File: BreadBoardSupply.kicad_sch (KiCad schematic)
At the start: 17 parts, among them J1 Barrel_Jack_Switch, J2 Conn_01x02_Male, J3 Conn_01x03_Male, J4 Screw_Terminal_01x02, J5 Conn_01x02_Male, J6 Conn_01x03_Male, J7 Screw_Terminal_01x02, U1 LM7805_TO220, U2 LM317_TO-220

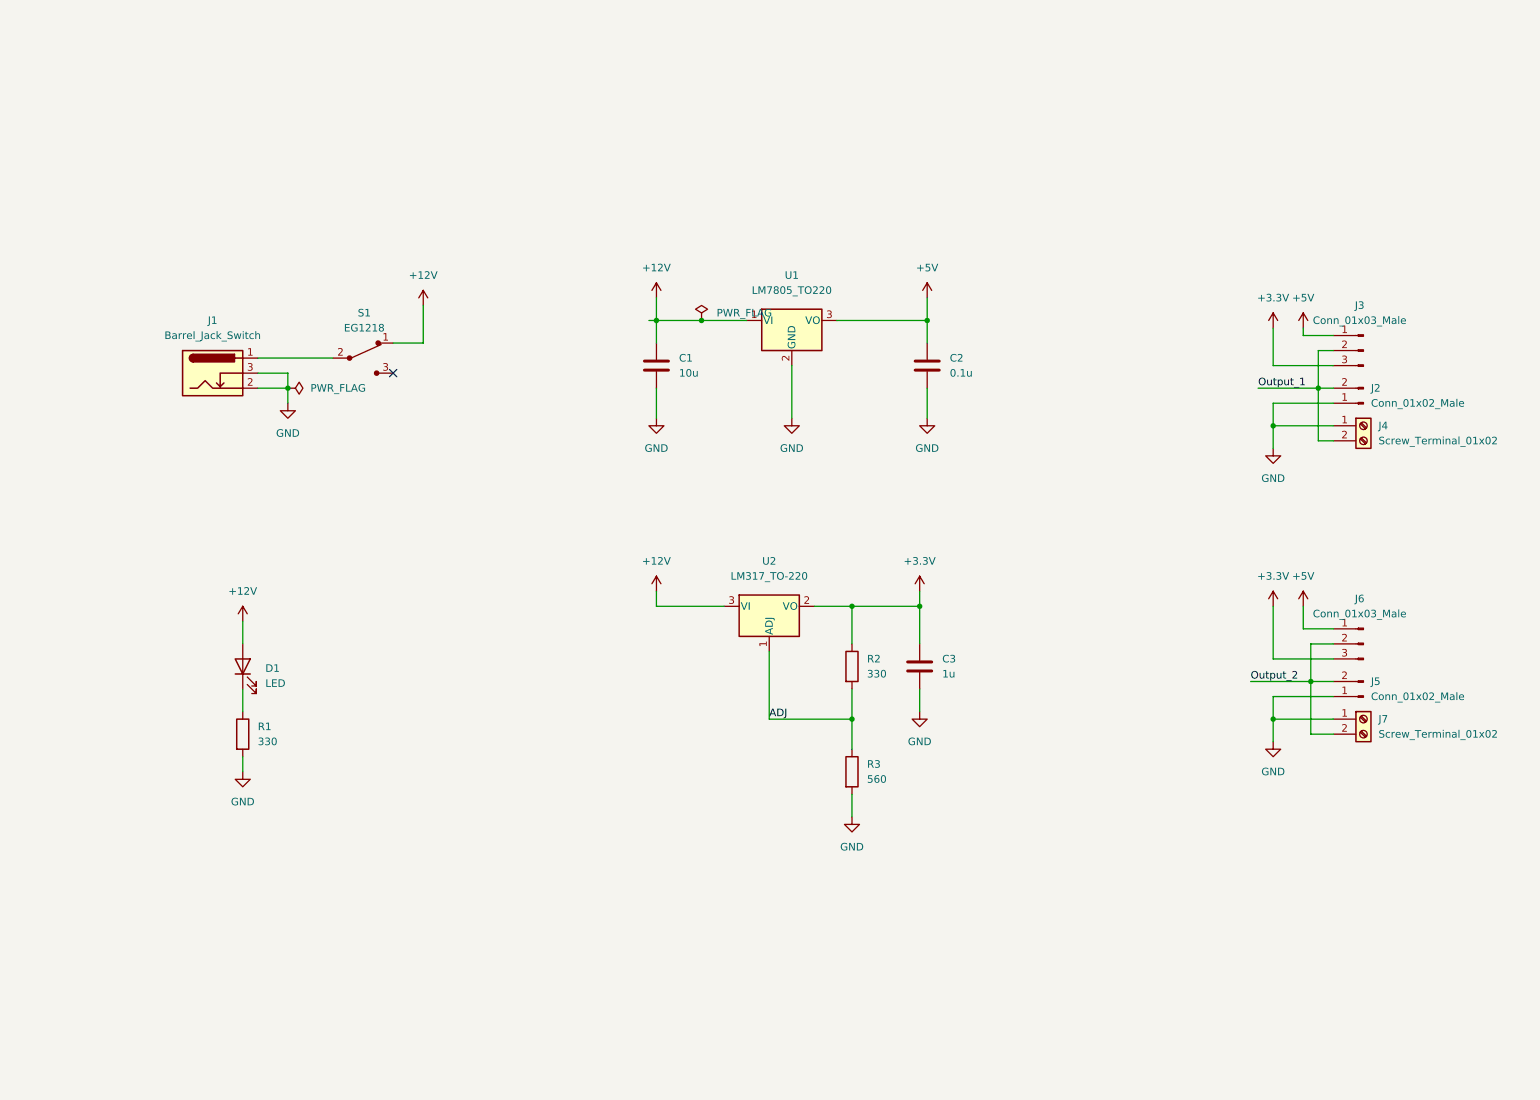
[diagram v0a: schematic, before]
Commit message: changed the footprints of some components, modified the regulator circuit
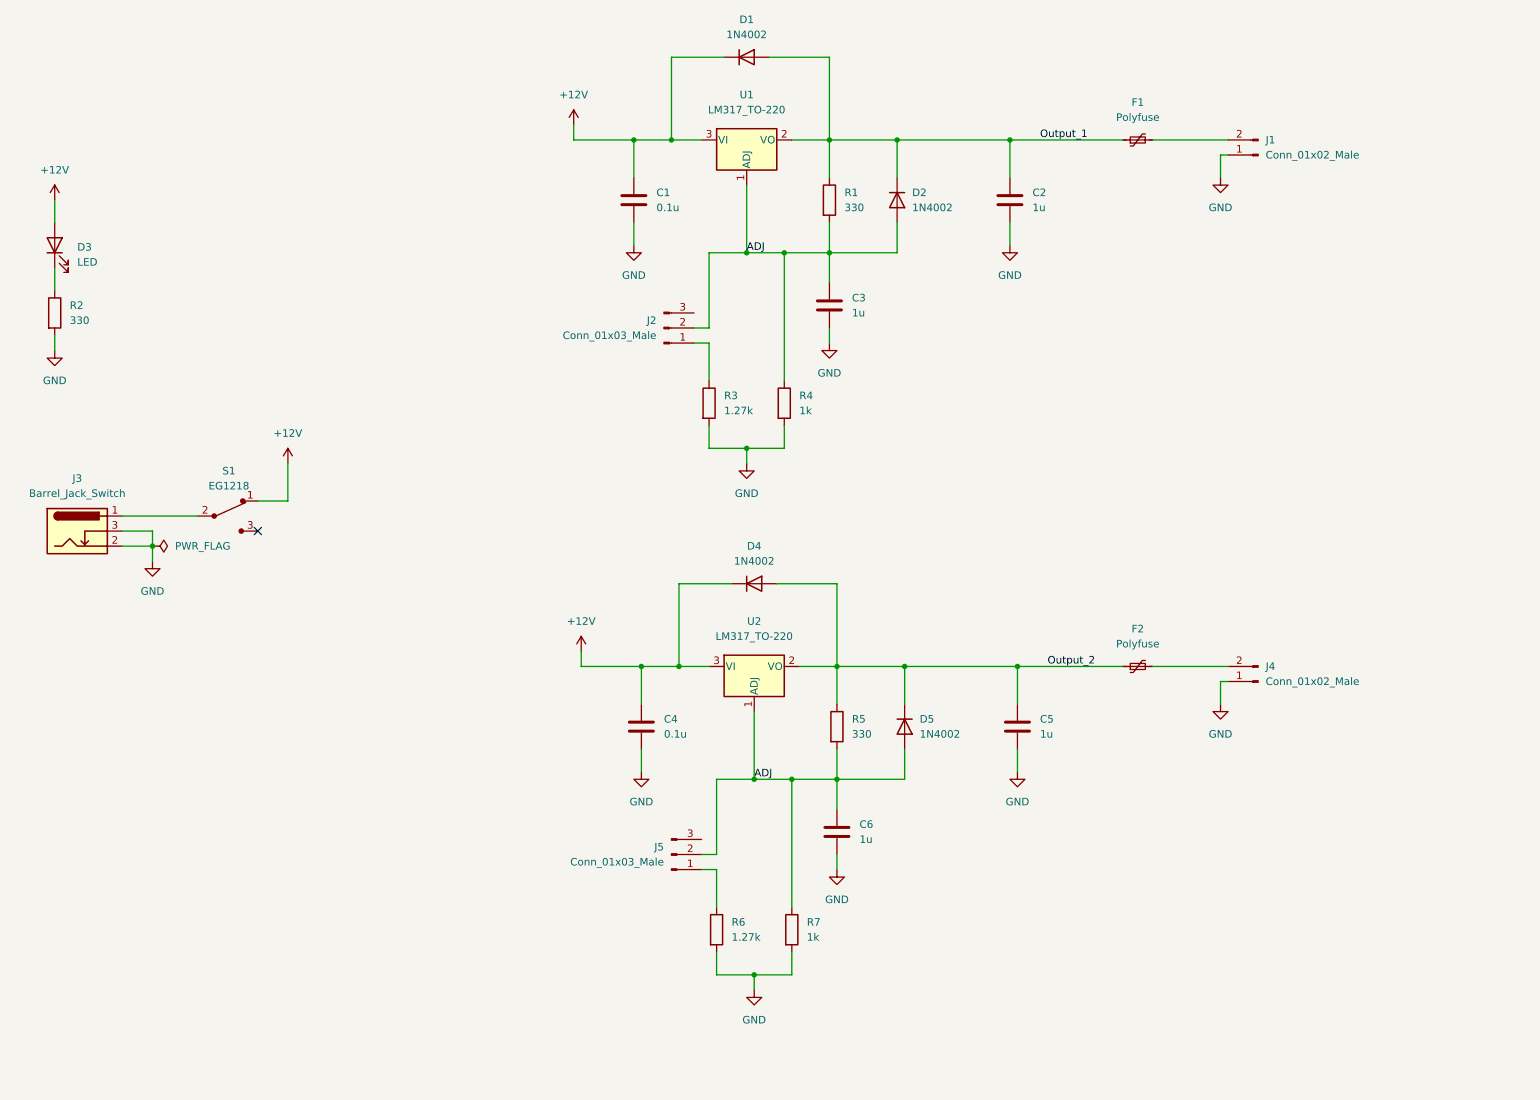
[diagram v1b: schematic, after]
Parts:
- removed J2: Conn_01x02_Male, Connector_PinHeader_2.54mm:PinHeader_1x02_P2.54mm_Vertical, symbol Connector:Conn_01x02_Male
- removed J3, J6: Conn_01x03_Male, Connector_PinHeader_2.54mm:PinHeader_1x03_P2.54mm_Vertical, symbol Connector:Conn_01x03_Male
- removed J4, J7: Screw_Terminal_01x02, TerminalBlock:TerminalBlock_bornier-2_P5.08mm, symbol Connector:Screw_Terminal_01x02
- removed U1: LM7805_TO220, Package_TO_SOT_THT:TO-220-3_Vertical, symbol Regulator_Linear:LM7805_TO220
- added C3, C6: 1u, Capacitor_THT:C_Disc_D3.0mm_W1.6mm_P2.50mm, symbol Device:C
- added C4: 0.1u, Capacitor_THT:C_Disc_D3.0mm_W1.6mm_P2.50mm, symbol Device:C
- added D1, D2, D4, D5: 1N4002, Diode_THT:D_DO-41_SOD81_P10.16mm_Horizontal, symbol Diode:1N4002
- added F1, F2: Polyfuse, symbol Device:Polyfuse_Small
- added J1: Conn_01x02_Male, Connector_PinHeader_2.54mm:PinHeader_1x02_P2.54mm_Vertical, symbol Connector:Conn_01x02_Male
- added J2, J5: Conn_01x03_Male, Connector_PinHeader_2.54mm:PinHeader_1x03_P2.54mm_Vertical, symbol Connector:Conn_01x03_Male
- added R1: 330, Resistor_THT:R_Axial_DIN0204_L3.6mm_D1.6mm_P7.62mm_Horizontal, symbol Device:R
- added R4, R7: 1k, Resistor_THT:R_Axial_DIN0204_L3.6mm_D1.6mm_P7.62mm_Horizontal, symbol Device:R
- added R6: 1.27k, Resistor_THT:R_Axial_DIN0204_L3.6mm_D1.6mm_P7.62mm_Horizontal, symbol Device:R
- added U1: LM317_TO-220, Package_TO_SOT_THT:TO-220-3_Vertical, symbol Regulator_Linear:LM317_TO-220
- C1: value 10u -> 0.1u
- C2: value 0.1u -> 1u
- R3: value 560 -> 1.27k
- renumbered C3 to C5, D1 to D3, J1 to J3, J5 to J4, R1 to R2, R2 to R5
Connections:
- net +3.3V is gone; now on net Output_2: C5.1, R5.1, U2.2 (VO)
- net +5V is gone; now on net Output_1: C2.1
- net +12V: now also C4.1, D1.1 (K), D4.1 (K), U1.3 (VI)
- net ADJ: now also C3.1, C6.1, D2.2 (A), D5.2 (A), J2.2 (Pin_2), J5.2 (Pin_2), R1.2, R4.1, R7.1, U1.1 (ADJ); no longer R3.1
- net GND: now also C3.2, C4.2, C6.2, J1.1 (Pin_1), R4.2, R6.2, R7.2
- net Output_1: now also D1.2 (A), D2.1 (K), F1.1, R1.1, U1.2 (VO)
- net Output_2: now also D4.2 (A), D5.1 (K), F2.1; no longer J4.2 (Pin_2)
- new net: J2.1 (Pin_1), R3.1
- new net: F2.2, J4.2 (Pin_2)
- new net: F1.2, J1.2 (Pin_2)
- new net: J5.1 (Pin_1), R6.1
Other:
- moved on the sheet: C5, D3, J3, J4, R2, R5, S1, U2

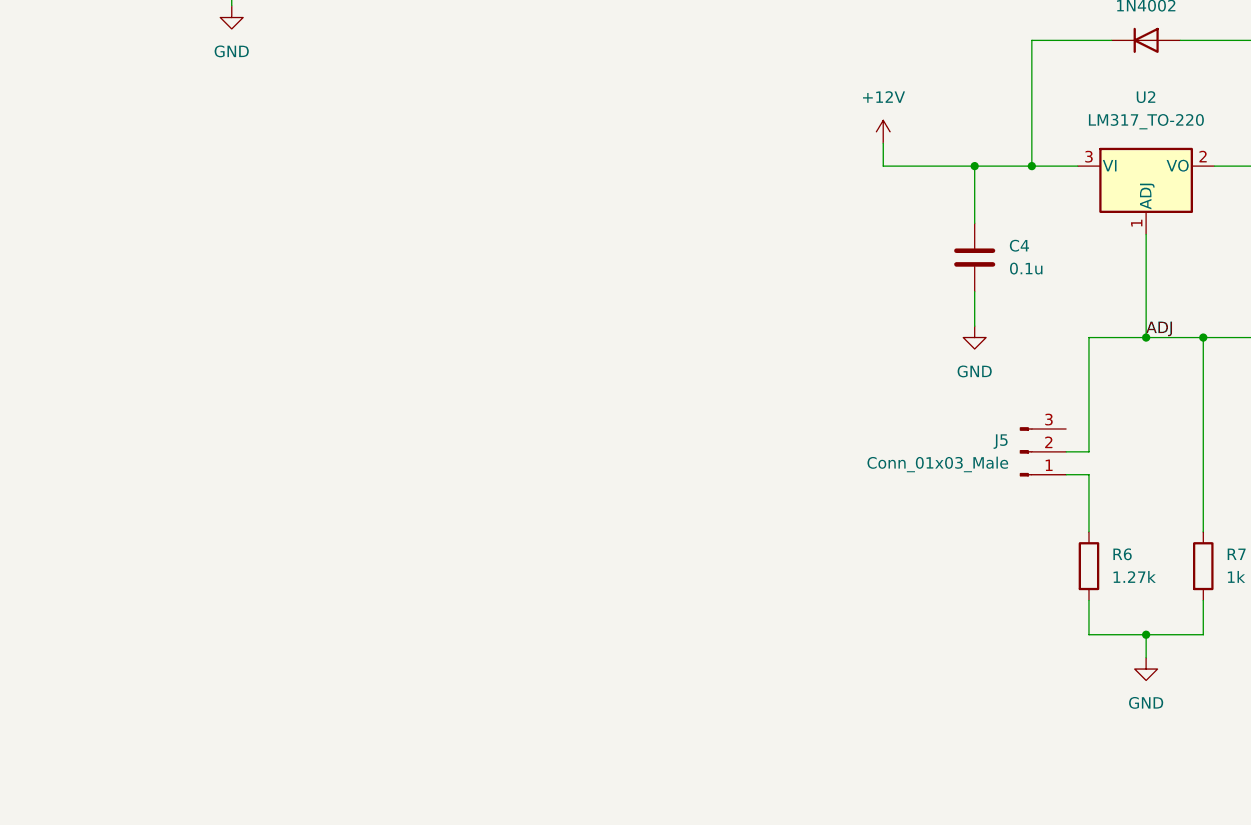
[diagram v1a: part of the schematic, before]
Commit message: not done but added some essential parts for the microUSB port
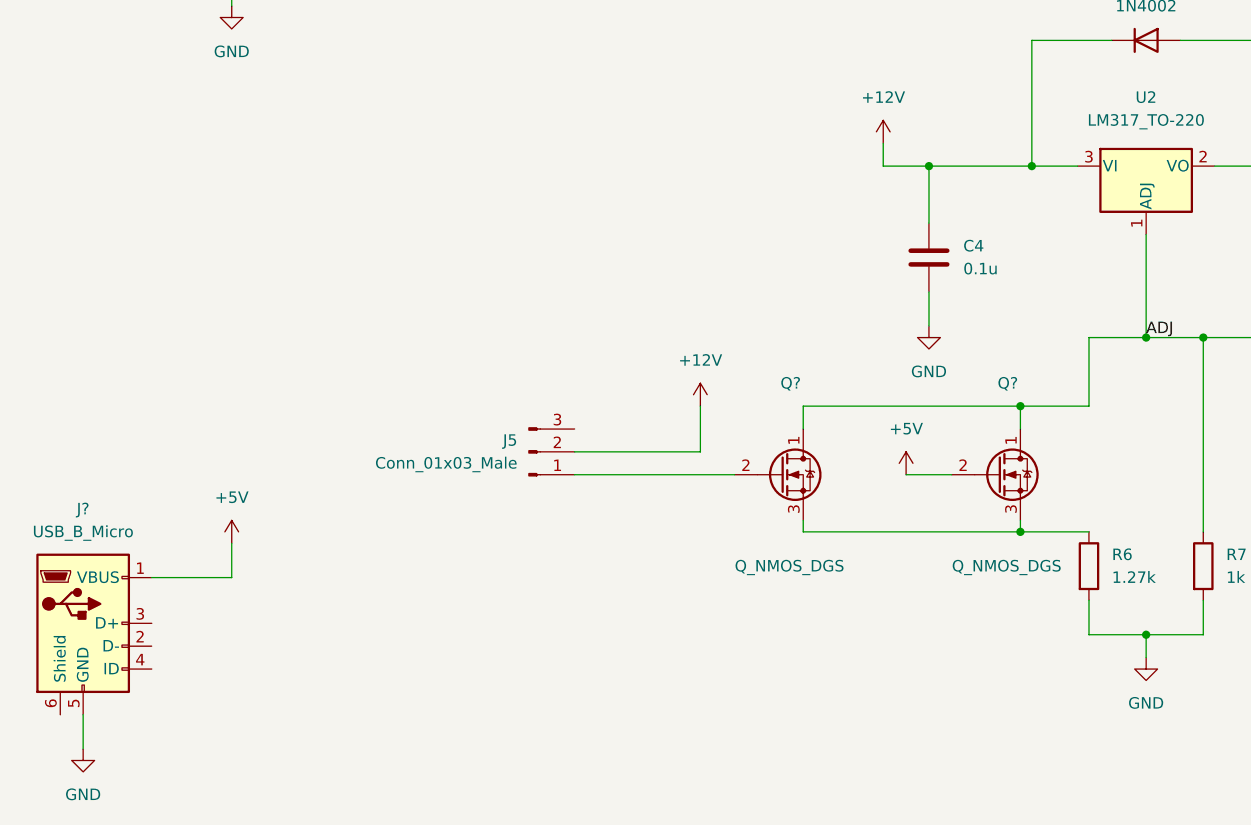
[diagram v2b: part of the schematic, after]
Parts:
- added J?: USB_B_Micro, symbol Connector:USB_B_Micro
- added Q? (x2): Q_NMOS_DGS, symbol Device:Q_NMOS_DGS
- C1, C2, C3: footprint Capacitor_THT:C_Disc_D3.0mm_W1.6mm_P2.50mm -> Capacitor_SMD:C_0805_2012Metric_Pad1.18x1.45mm_HandSolder
- D1: footprint Diode_THT:D_DO-41_SOD81_P10.16mm_Horizontal -> LED_SMD:LED_0805_2012Metric_Pad1.15x1.40mm_HandSolder
- J1: footprint Connector_PinHeader_2.54mm:PinHeader_1x02_P2.54mm_Vertical -> Connector_BarrelJack:BarrelJack_Horizontal
- J2, J5: footprint Connector_PinHeader_2.54mm:PinHeader_1x03_P2.54mm_Vertical -> Connector_PinHeader_2.54mm:PinHeader_1x02_P2.54mm_Vertical
- J3: footprint Connector_BarrelJack:BarrelJack_Horizontal -> Connector_PinHeader_2.54mm:PinHeader_1x03_P2.54mm_Vertical
- J4: footprint Connector_PinHeader_2.54mm:PinHeader_1x02_P2.54mm_Vertical -> TerminalBlock:TerminalBlock_bornier-2_P5.08mm
- R1, R2, R3: footprint Resistor_THT:R_Axial_DIN0204_L3.6mm_D1.6mm_P7.62mm_Horizontal -> Resistor_SMD:R_0805_2012Metric_Pad1.20x1.40mm_HandSolder
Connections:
- net +12V: now also J5.2 (Pin_2)
- net ADJ: now also Q?.1 (D), Q?.1 (D); no longer J5.2 (Pin_2)
- net GND: now also J?.5 (GND)
- net at J5.1 (Pin_1): now also Q?.2 (G); no longer R6.1
- new net: Q?.3 (S), Q?.3 (S), R6.1
- new net +5V: J?.1 (VBUS), Q?.2 (G)
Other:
- moved on the sheet: C4, J5
